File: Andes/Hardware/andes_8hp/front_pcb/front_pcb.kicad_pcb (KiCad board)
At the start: 2 copper layers, 40 x 110 mm, 30 parts, among them J11 out1, J12 out2, J2 Conn_02x12_Odd_Even, J3 CV1, J4 CV2, J5 CV3, J6 CV4, J7 in1, J8 in2, J9 Conn_02x08_Odd_Even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

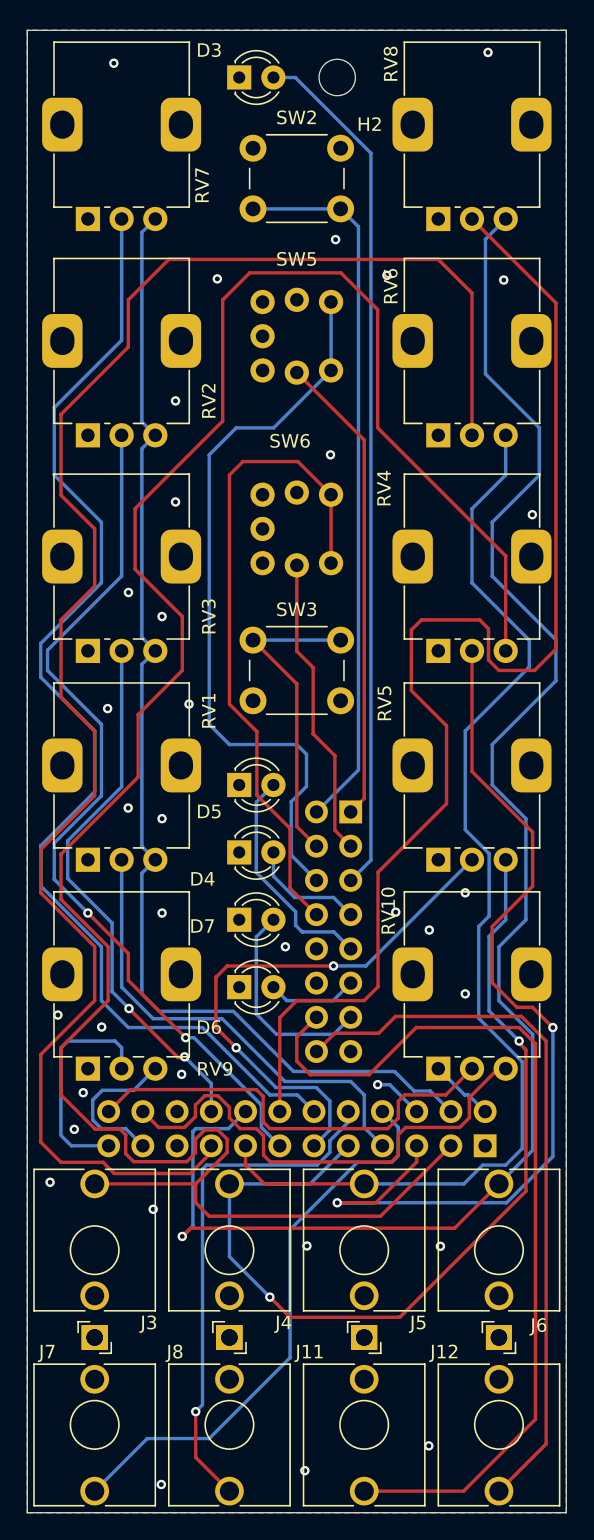
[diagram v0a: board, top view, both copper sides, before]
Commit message: [Andes 8HP] Fix floating copper, swap some LEDs and potmeter
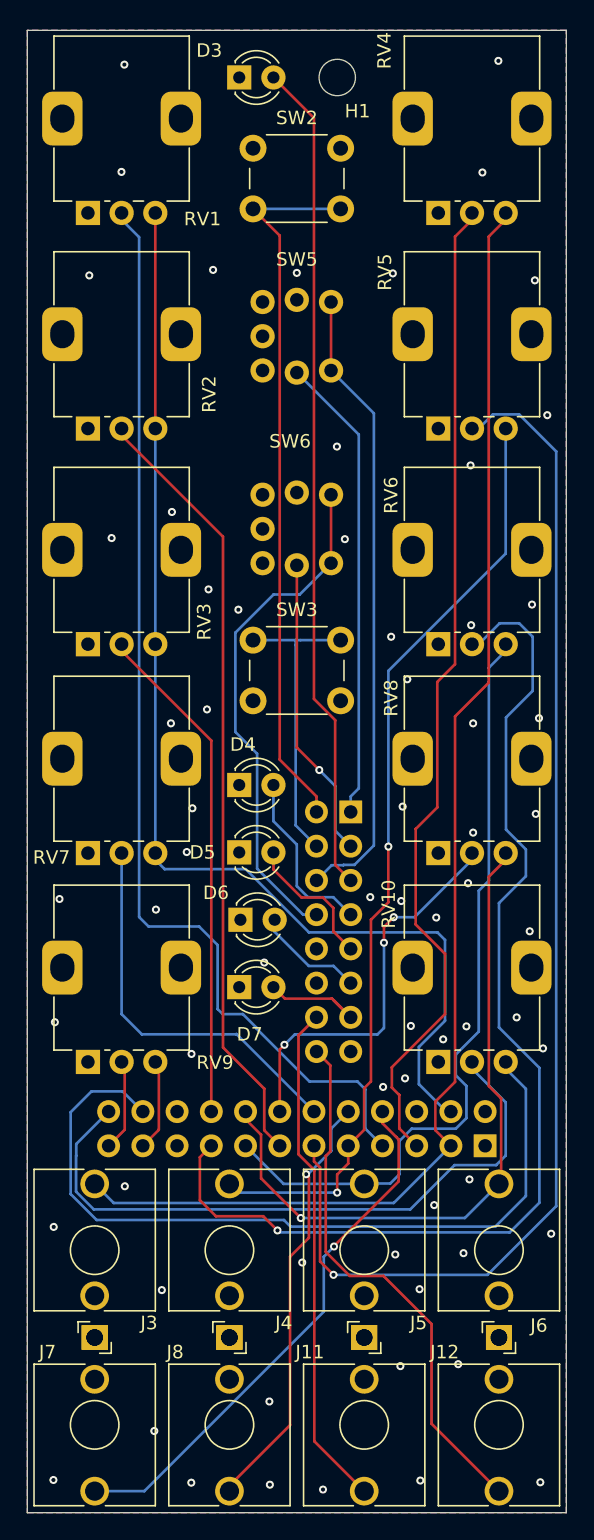
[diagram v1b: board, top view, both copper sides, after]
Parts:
- removed H2: MountingHole, MountingHole:MountingHole_2.7mm_M2.5
- added H1: MountingHole, MountingHole:MountingHole_2.7mm_M2.5, F.Cu at (149.5, 46.5)
- moved RV1 48.0 mm to (131.0, 56.5)
- moved RV7 47.0 mm to (131.0, 104.0)
- moved RV8 47.0 mm to (157.0, 104.0)
- moved RV4 32.5 mm to (157.0, 56.5)
- moved RV5 32.0 mm to (157.0, 72.5)
- moved RV6 15.5 mm to (157.0, 88.5)
- moved D6 5.00 mm to (142.3, 109.0)
- moved D4 5.00 mm to (142.2, 99.0)
- moved D5 5.00 mm to (142.2, 104.0)
- moved D7 5.00 mm to (142.2, 114.0)
- moved RV10 0.50 mm to (157.0, 119.5)
- moved RV2 0.50 mm to (131.0, 72.5)
- moved RV3 0.50 mm to (131.0, 88.5)
- moved RV9 0.50 mm to (131.0, 119.5)
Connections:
- D3 pad 1: (no net) -> GND1
- D3 pad 2: (no net) -> /LED1
- D4 pad 1: (no net) -> GND1
- D4 pad 2: (no net) -> /LED2
- D5 pad 1: (no net) -> GND1
- D5 pad 2: (no net) -> /LED3
- D6 pad 1: (no net) -> GND1
- D6 pad 2: (no net) -> /LED4
- D7 pad 1: (no net) -> GND1
- D7 pad 2: (no net) -> /LED5
- J11 pad S: (no net) -> GND1
- J11 pad T: (no net) -> /OUT1
- J11 pad TN: (no net) -> unconnected-(J11-PadTN)
- J12 pad S: (no net) -> GND1
- J12 pad T: (no net) -> /OUT2
- J12 pad TN: (no net) -> unconnected-(J12-PadTN)
- J2 pad 1: (no net) -> GND1
- J2 pad 10: (no net) -> /TRIG_2
- J2 pad 11: (no net) -> /CV2_ATVPOT
- J2 pad 12: (no net) -> /CV4_POT
- J2 pad 13: (no net) -> /CV2_POT
- J2 pad 14: (no net) -> /CV4_ATVPOT
- J2 pad 15: (no net) -> /CV3_JACK
- J2 pad 16: (no net) -> /CV4_JACK
- J2 pad 17: (no net) -> /CV3_ATVPOT
- J2 pad 18: (no net) -> /CV3_POT
- J2 pad 19: (no net) -> GND1
- J2 pad 2: (no net) -> GND1
- J2 pad 20: (no net) -> GND1
- J2 pad 21: (no net) -> /PRE_ATV_OUT1
- J2 pad 22: (no net) -> /PRE_ATV_OUT2
- J2 pad 23: (no net) -> /OUT1_ATVPOT
- J2 pad 24: (no net) -> /OUT2_ATVPOT
- J2 pad 3: (no net) -> /CV1_JACK
- J2 pad 4: (no net) -> /-10V_REF
- J2 pad 5: (no net) -> /CV1_ATVPOT
- J2 pad 6: (no net) -> GND1
- J2 pad 7: (no net) -> /CV1_POT
- J2 pad 8: (no net) -> /TRIG_1
- J2 pad 9: (no net) -> /CV2_JACK
- J3 pad S: (no net) -> GND1
- J3 pad T: (no net) -> /CV1_JACK
- J3 pad TN: (no net) -> GND1
- J4 pad S: (no net) -> GND1
- J4 pad T: (no net) -> /CV2_JACK
- J4 pad TN: (no net) -> GND1
- J5 pad S: (no net) -> GND1
- J5 pad T: (no net) -> /CV3_JACK
- J5 pad TN: (no net) -> GND1
- J6 pad S: (no net) -> GND1
- J6 pad T: (no net) -> /CV4_JACK
- J6 pad TN: (no net) -> GND1
- J7 pad S: (no net) -> GND1
- J7 pad T: (no net) -> /TRIG_1
- J7 pad TN: (no net) -> GND1
- J8 pad S: (no net) -> GND1
- J8 pad T: (no net) -> /TRIG_2
- J8 pad TN: (no net) -> GND1
- J9 pad 1: (no net) -> /LED_SALIDA_1
- J9 pad 10: (no net) -> GND1
- J9 pad 11: (no net) -> /LED4
- J9 pad 12: (no net) -> GND1
- J9 pad 13: (no net) -> /LED5
- J9 pad 14: (no net) -> /OUT1
- J9 pad 15: (no net) -> GND1
- J9 pad 16: (no net) -> /OUT2
- J9 pad 2: (no net) -> /SW_DUAL
- J9 pad 3: (no net) -> /LED_SALIDA_2
- J9 pad 4: (no net) -> /SW_MODE
- J9 pad 5: (no net) -> /LED1
- J9 pad 6: (no net) -> /SW_TRIG1
- J9 pad 7: (no net) -> /LED2
- J9 pad 8: (no net) -> /SW_TRIG2
- J9 pad 9: (no net) -> /LED3
- RV1 pad 1: (no net) -> GND1
- RV1 pad 2: (no net) -> /CV1_POT
- RV1 pad 3: (no net) -> /-10V_REF
- RV10 pad 1: (no net) -> GND1
- RV10 pad 2: (no net) -> /OUT2_ATVPOT
- RV10 pad 3: (no net) -> /PRE_ATV_OUT2
- RV2 pad 1: (no net) -> GND1
- RV2 pad 2: (no net) -> /CV2_POT
- RV2 pad 3: (no net) -> /-10V_REF
- RV3 pad 1: (no net) -> GND1
- RV3 pad 2: (no net) -> /CV3_POT
- RV3 pad 3: (no net) -> /-10V_REF
- RV4 pad 1: (no net) -> GND1
- RV4 pad 2: (no net) -> /CV1_ATVPOT
- RV4 pad 3: (no net) -> /CV1_JACK
- RV5 pad 1: (no net) -> GND1
- RV5 pad 2: (no net) -> /CV2_ATVPOT
- RV5 pad 3: (no net) -> /CV2_JACK
- RV6 pad 1: (no net) -> GND1
- RV6 pad 2: (no net) -> /CV3_ATVPOT
- RV6 pad 3: (no net) -> /CV3_JACK
- RV7 pad 1: (no net) -> GND1
- RV7 pad 2: (no net) -> /CV4_POT
- RV7 pad 3: (no net) -> /-10V_REF
- RV8 pad 1: (no net) -> GND1
- RV8 pad 2: (no net) -> /CV4_ATVPOT
- RV8 pad 3: (no net) -> /CV4_JACK
- RV9 pad 1: (no net) -> GND1
- RV9 pad 2: (no net) -> /OUT1_ATVPOT
- RV9 pad 3: (no net) -> /PRE_ATV_OUT1
- SW2 pad 1: (no net) -> /SW_DUAL
- SW2 pad 2: (no net) -> GND1
- SW3 pad 1: (no net) -> /SW_MODE
- SW3 pad 2: (no net) -> GND1
- SW5 pad 1: (no net) -> /SW_TRIG1
- SW5 pad 2: (no net) -> /SW_TRIG1
- SW5 pad 3: (no net) -> GND1
- SW5 pad 4: (no net) -> GND1
- SW5 pad L1: (no net) -> /LED_SALIDA_1
- SW5 pad L2: (no net) -> GND1
- SW6 pad 1: (no net) -> /SW_TRIG2
- SW6 pad 2: (no net) -> /SW_TRIG2
- SW6 pad 3: (no net) -> GND1
- SW6 pad 4: (no net) -> GND1
- SW6 pad L1: (no net) -> /LED_SALIDA_2
- SW6 pad L2: (no net) -> GND1
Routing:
- net (no net): track 1742.6 -> 0.00 mm, vias 47 -> 0
- net /CV1_JACK: track 0.00 -> 100.1 mm
- net /CV2_ATVPOT: track 0.00 -> 92.8 mm, vias 0 -> 1
- net /-10V_REF: track 0.00 -> 86.2 mm
- net /CV3_ATVPOT: track 0.00 -> 82.7 mm, vias 0 -> 1
- net /CV1_POT: track 0.00 -> 81.9 mm
- net /CV1_ATVPOT: track 0.00 -> 73.8 mm
- net /CV2_JACK: track 0.00 -> 69.6 mm, vias 0 -> 2
- net /LED1: track 0.00 -> 62.0 mm
- net /PRE_ATV_OUT2: track 0.00 -> 58.5 mm
- net /CV3_JACK: track 0.00 -> 57.6 mm
- net /CV2_POT: track 0.00 -> 57.6 mm
- net /SW_DUAL: track 0.00 -> 53.2 mm
- net /CV4_JACK: track 0.00 -> 50.4 mm, vias 0 -> 1
- net /OUT2_ATVPOT: track 0.00 -> 48.5 mm
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- added copper zone on B.Cu, net GND1
- added copper zone on F.Cu, net GND1
- removed copper zone on B.Cu, net (none)
- removed copper zone on F.Cu, net (none)

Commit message: Fix attenuverter inversion, generate new gerber, update .gitignore
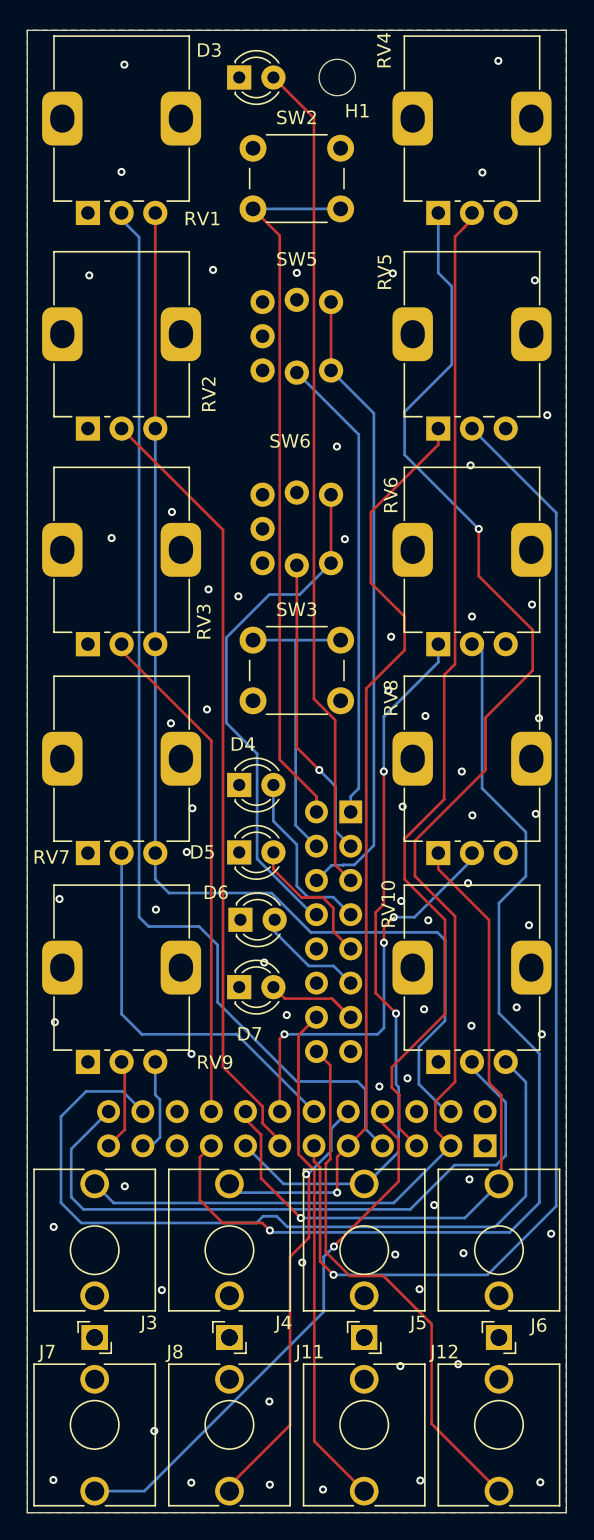
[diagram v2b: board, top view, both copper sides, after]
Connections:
- RV4 pad 1: GND1 -> /CV1_JACK
- RV4 pad 3: /CV1_JACK -> GND1
- RV5 pad 1: GND1 -> /CV2_JACK
- RV5 pad 3: /CV2_JACK -> GND1
- RV6 pad 1: GND1 -> /CV3_JACK
- RV6 pad 3: /CV3_JACK -> GND1
- RV8 pad 1: GND1 -> /CV4_JACK
- RV8 pad 3: /CV4_JACK -> GND1
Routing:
- net /CV1_JACK: track 100.1 -> 109.7 mm, vias 0 -> 1
- net /CV3_ATVPOT: track 82.7 -> 78.5 mm
- net /CV3_JACK: track 57.6 -> 53.9 mm, vias 0 -> 2
- net /PRE_ATV_OUT2: track 58.5 -> 61.0 mm
- net /CV1_ATVPOT: track 73.8 -> 75.8 mm
- net /-10V_REF: track 86.2 -> 88.0 mm
- net /CV2_ATVPOT: track 92.8 -> 91.0 mm
- net /CV4_JACK: track 50.4 -> 51.9 mm
- net /OUT2_ATVPOT: track 48.5 -> 49.8 mm
- net /CV4_ATVPOT: track 29.1 -> 30.1 mm
- net /PRE_ATV_OUT1: track 6.32 -> 7.28 mm
- net /CV2_JACK: track 69.6 -> 70.1 mm, vias 2 -> 1
- net /CV2_POT: track 57.6 -> 58.1 mm
- net /OUT1_ATVPOT: track 6.31 -> 6.81 mm
- net /CV4_POT: track 28.7 -> 29.2 mm
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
